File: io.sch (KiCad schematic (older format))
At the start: 36 parts

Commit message: Se hace cambios en el esquematico y se anexa PCB
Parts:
- removed J? (x4): Conn_01x02, symbol Connector:Conn_01x02_Female
- removed M? (x8): MNMOS, symbol pspice:MNMOS
- added J503: Conn_01x06_Male, Connector_PinHeader_1.27mm:PinHeader_1x06_P1.27mm_Vertical, symbol Connector:Conn_01x06_Male
- added Q501, Q502, Q503, Q504, Q505, Q506, Q507, Q508: FDV301N, Package_TO_SOT_SMD:SOT-23, symbol Device:Q_NMOS_GDS
- D501, D502, D503, D504, D505, D506, D507, D508: renamed from D?; footprint (none) -> Diode_SMD:D_0805_2012Metric_Pad1.15x1.40mm_HandSolder
- J501, J502: renamed from J?; footprint (none) -> Connector_PinHeader_1.00mm:PinHeader_2x20_P1.00mm_Vertical
- J504, J505: renamed from J?; footprint (none) -> Connector_PinHeader_1.27mm:PinHeader_1x04_P1.27mm_Vertical
- R501, R502, R503, R504, R505, R506, R507, R508, R509, R510, R511, R512: renamed from R?; footprint (none) -> Resistor_SMD:R_0805_2012Metric_Pad1.15x1.40mm_HandSolder
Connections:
- net labels added: COMM0, COMM1, COMM2, COMM3, COMM[0..3], I2C0, I2C1, I2C[0..1], LED0, LED1, LED2, LED3, LED4, LED5, LED6, LED7, LED[0..7], PWM_OUT0, PWM_OUT1, PWM_OUT2, PWM_OUT3, SW0, SW1, SW2, SW3, SW4, SW5, SW6, SW7, SW[0..7]
- wire segments 128 -> 148
- no-connect marks 0 -> 42
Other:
- moved on the sheet: D501, D502, D503, D504, J501, J502, R501, R502, R503, R504

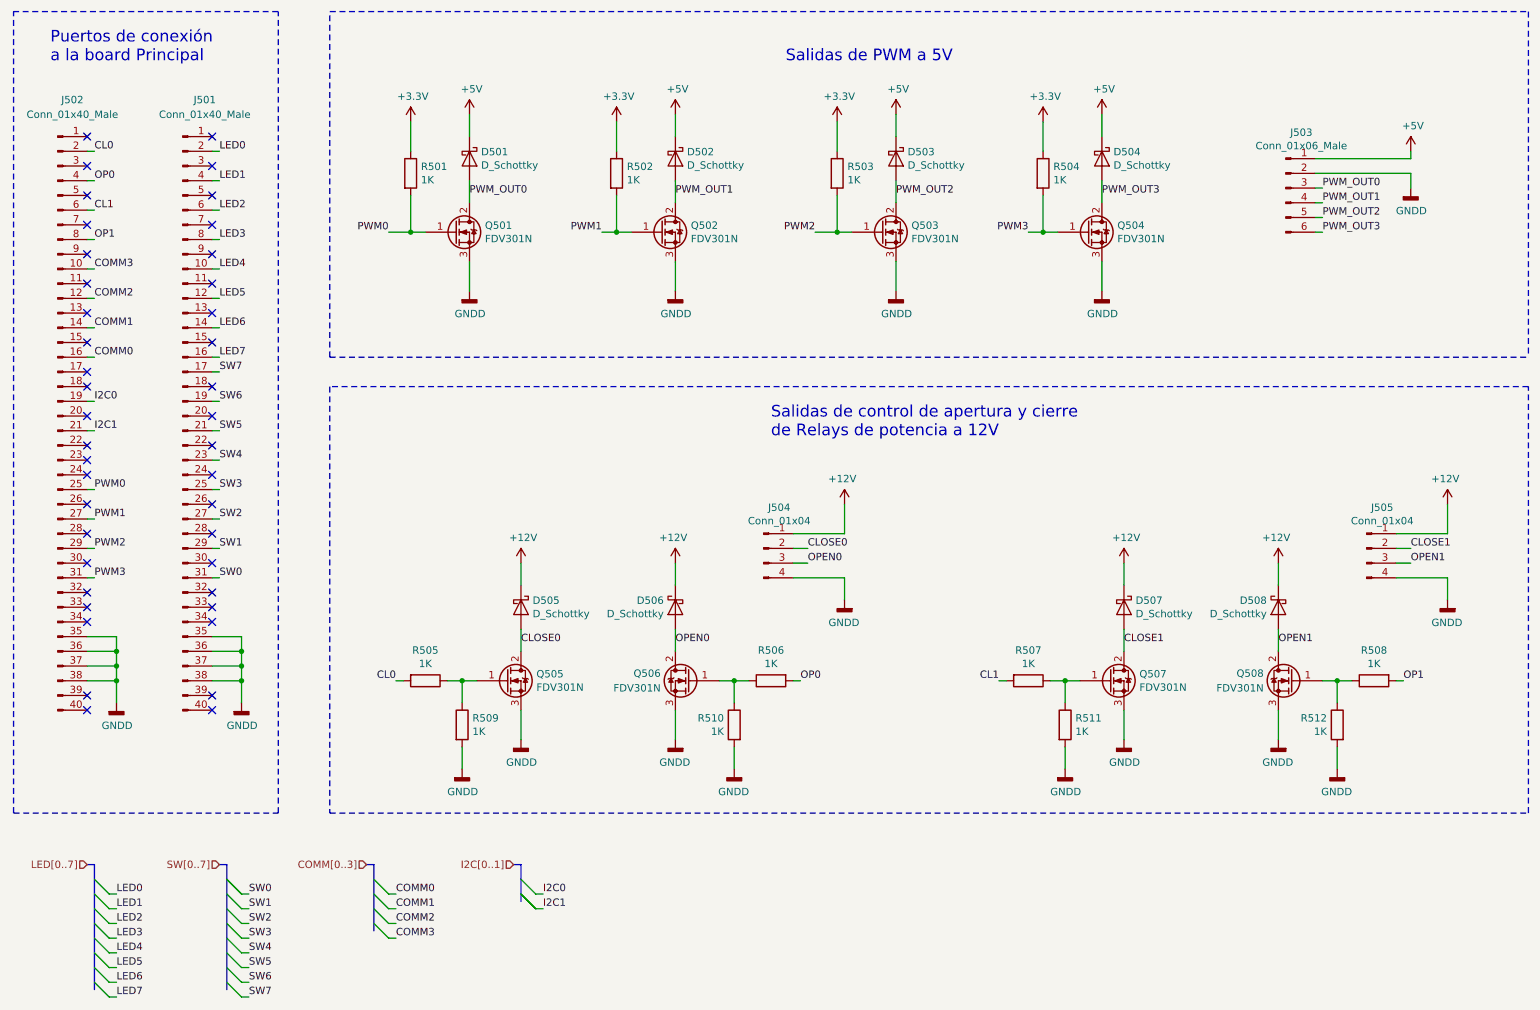
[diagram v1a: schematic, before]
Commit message: Se realizan correcciones finales y se agregan carpetas BOM, Datasheet, Doc, Gerbers, lib.pretty y shapes3D
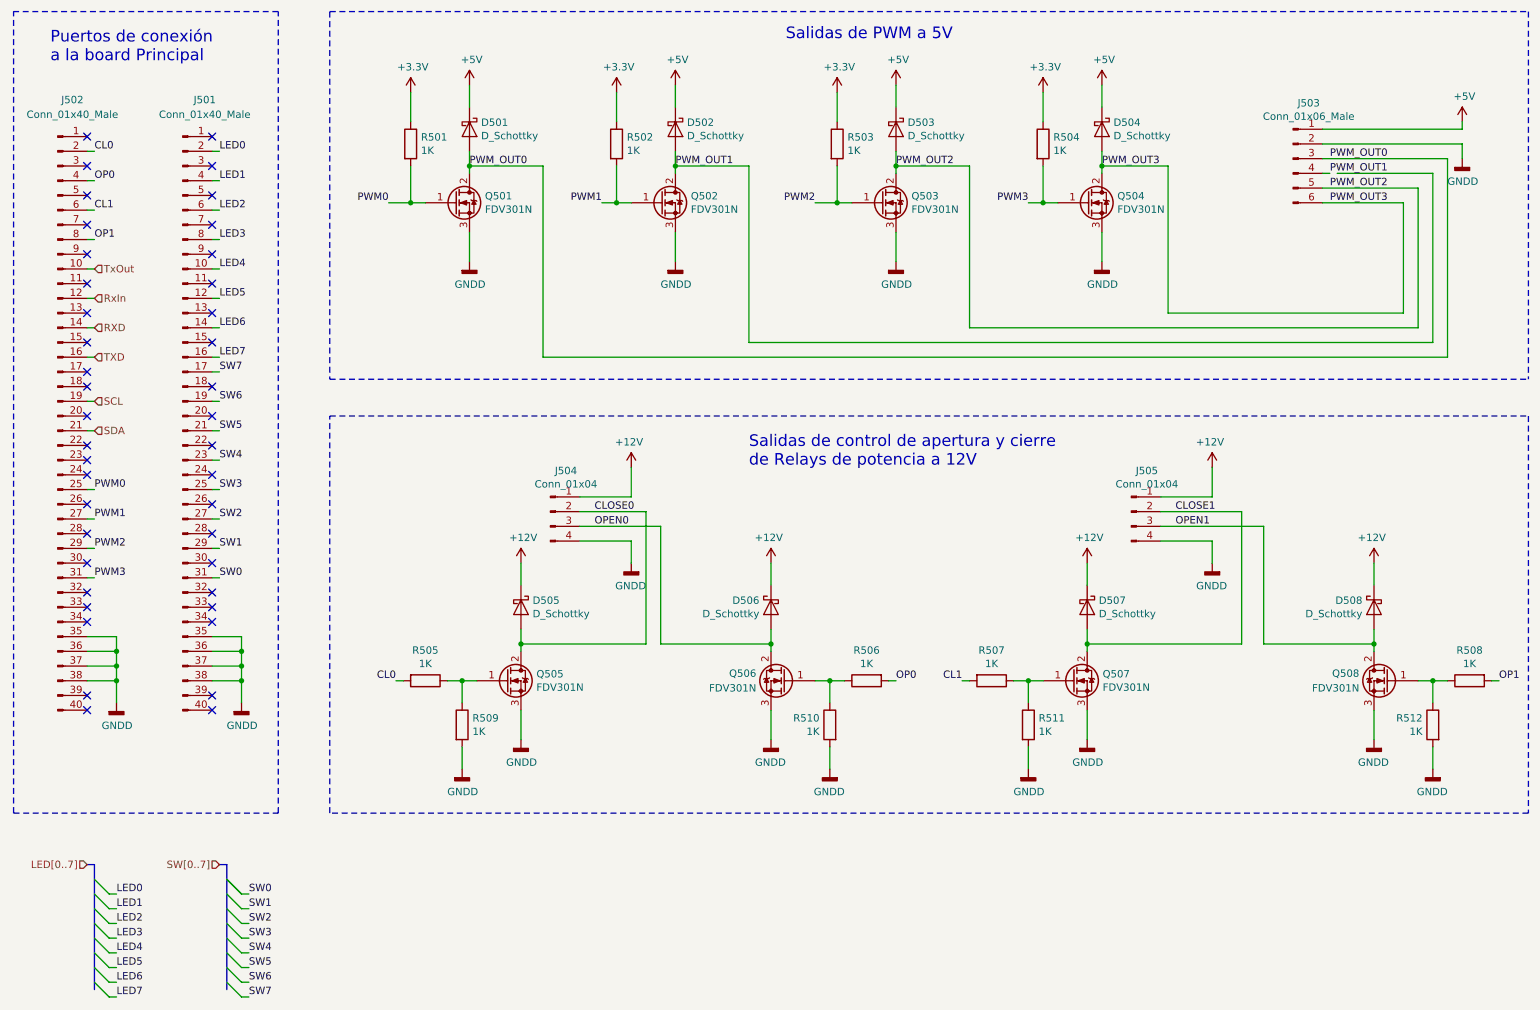
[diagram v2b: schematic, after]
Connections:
- net COMM0 renamed TXD
- net COMM1 renamed RXD
- net COMM2 renamed RxIn
- net COMM3 renamed TxOut
- net I2C0 renamed SCL
- net I2C1 renamed SDA
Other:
- moved on the sheet: D501, D502, D503, D504, D506, D507, D508, J503, J504, J505, Q501, Q502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
